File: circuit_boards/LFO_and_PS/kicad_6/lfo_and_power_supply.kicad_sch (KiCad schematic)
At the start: 17 parts, among them J1 AC_power_in, J2 power_out, J3 power_out, J4 power_out, J5 power_out, J6 filter_board_port, U1 TL072

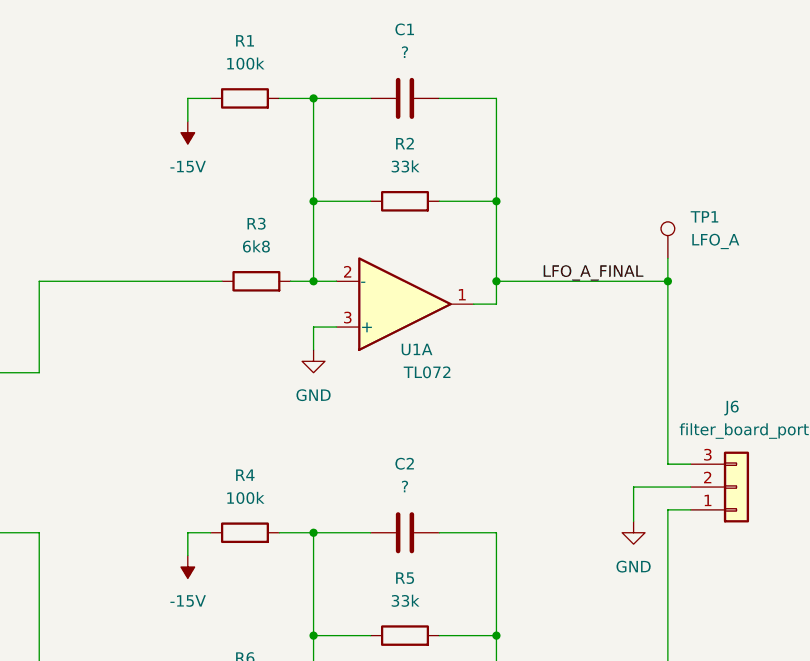
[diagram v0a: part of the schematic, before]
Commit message: Update PCB files, fix VCF mix polarity
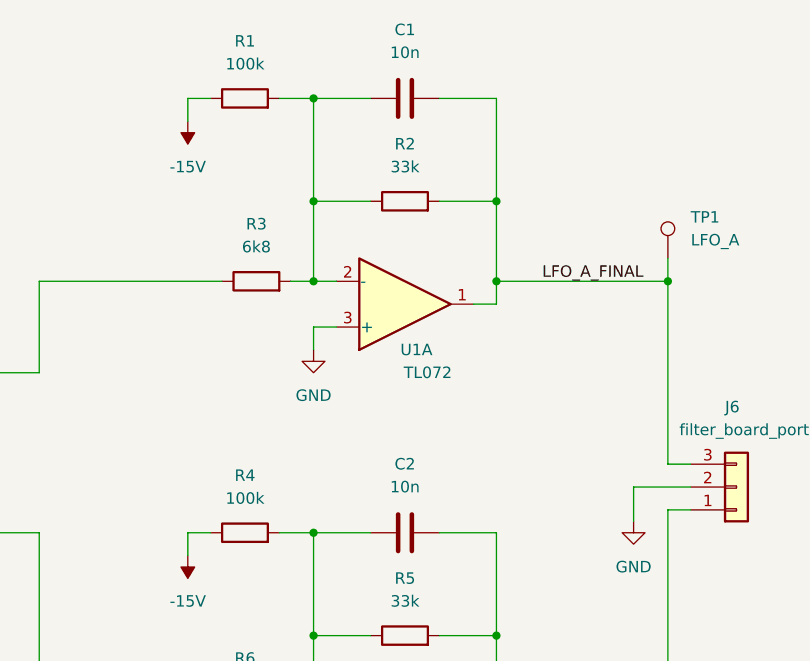
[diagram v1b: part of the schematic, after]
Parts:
- C1, C2: value ? -> 10n
- J1: footprint Connector_Molex:Molex_Mini-Fit_Jr_5566-04A2_2x02_P4.20mm_Vertical -> Connector_Molex:Molex_Mini-Fit_Jr_5566-04A_2x02_P4.20mm_Vertical
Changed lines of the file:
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@@
     (in_bom yes) (on_board yes) (fields_autoplaced)
     (property "Reference" "C2" (id 0) (at 190.5 82.55 90))
-    (property "Value" "?" (id 1) (at 190.5 85.09 90))
+    (property "Value" "10n" (id 1) (at 190.5 85.09 90))
     (property "Footprint" "Capacitor_SMD:C_0805_2012Metric" (id 2) (at 194.31 89.2048 0)
       (effects (font (size 1.27 1.27)) hide)
@@
     (in_bom yes) (on_board yes) (fields_autoplaced)
     (property "Reference" "C1" (id 0) (at 190.5 34.29 90))
-    (property "Value" "?" (id 1) (at 190.5 36.83 90))
+    (property "Value" "10n" (id 1) (at 190.5 36.83 90))
     (property "Footprint" "Capacitor_SMD:C_0805_2012Metric" (id 2) (at 194.31 40.9448 0)
       (effects (font (size 1.27 1.27)) hide)
@@
     (property "Reference" "J1" (id 0) (at 30.48 66.04 0))
     (property "Value" "AC_power_in" (id 1) (at 30.48 68.58 0))
-    (property "Footprint" "Connector_Molex:Molex_Mini-Fit_Jr_5566-04A2_2x02_P4.20mm_Vertical" (id 2) (at 30.48 74.93 0)
+    (property "Footprint" "Connector_Molex:Molex_Mini-Fit_Jr_5566-04A_2x02_P4.20mm_Vertical" (id 2) (at 30.48 74.93 0)
       (effects (font (size 1.27 1.27)) hide)
     )
@@
     )
     (path "/27a532ef-0c09-4c62-bfbb-3624ef1c7dcb"
-      (reference "C1") (unit 1) (value "?") (footprint "Capacitor_SMD:C_0805_2012Metric")
+      (reference "C1") (unit 1) (value "10n") (footprint "Capacitor_SMD:C_0805_2012Metric")
     )
     (path "/05e95b16-6b62-44ea-8a25-dc38df4ba710"
-      (reference "C2") (unit 1) (value "?") (footprint "Capacitor_SMD:C_0805_2012Metric")
+      (reference "C2") (unit 1) (value "10n") (footprint "Capacitor_SMD:C_0805_2012Metric")
     )
     (path "/6cc8d67d-f0af-4522-97bb-c57e963f3f9d/720fda08-e38e-4be5-beaa-b632b67d25fa"
@@
     )
     (path "/4cab5afe-b810-46b3-94ba-f613dce05909/6fab5011-5325-4ae8-afe8-6cd1a3fbb272"
-      (reference "C10") (unit 1) (value "3300u") (footprint "Capacitor_THT:CP_Radial_D17.0mm_P7.50mm")
+      (reference "C10") (unit 1) (value "3300u") (footprint "Capacitor_THT:CP_Radial_D18.0mm_P7.50mm")
     )
     (path "/4cab5afe-b810-46b3-94ba-f613dce05909/ffac9709-5007-4704-8f66-7b36093713ab"
@@
     )
     (path "/4cab5afe-b810-46b3-94ba-f613dce05909/30fa96ad-c9c9-4229-834c-2ec93d10420f"
-      (reference "C14") (unit 1) (value "3300u") (footprint "Capacitor_THT:CP_Radial_D17.0mm_P7.50mm")
+      (reference "C14") (unit 1) (value "3300u") (footprint "Capacitor_THT:CP_Radial_D18.0mm_P7.50mm")
     )
     (path "/4cab5afe-b810-46b3-94ba-f613dce05909/cbd0ff89-c284-432e-8a26-664af57066a8"
@@
     )
     (path "/aa436904-5524-429e-93cc-6d6a65f39f69"
-      (reference "J1") (unit 1) (value "AC_power_in") (footprint "Connector_Molex:Molex_Mini-Fit_Jr_5566-04A2_2x02_P4.20mm_Vertical")
+      (reference "J1") (unit 1) (value "AC_power_in") (footprint "Connector_Molex:Molex_Mini-Fit_Jr_5566-04A_2x02_P4.20mm_Vertical")
     )
     (path "/aeb3b2c9-24f9-4cdf-a26a-8ea198dfa225"
@@
     )
     (path "/6cc8d67d-f0af-4522-97bb-c57e963f3f9d/c1ca5964-b548-4f9e-b8b8-dbc4e7594301"
-      (reference "R7") (unit 1) (value "R") (footprint "Resistor_SMD:R_0805_2012Metric")
+      (reference "R7") (unit 1) (value "10k") (footprint "Resistor_SMD:R_0805_2012Metric")
     )
     (path "/6cc8d67d-f0af-4522-97bb-c57e963f3f9d/db1373b0-0aeb-4604-988a-b51417beff8b"
@@
     )
     (path "/6cc8d67d-f0af-4522-97bb-c57e963f3f9d/e656cab0-5f68-4d01-b288-557c94075e1f"
-      (reference "R9") (unit 1) (value "R") (footprint "Resistor_SMD:R_0805_2012Metric")
+      (reference "R9") (unit 1) (value "15k") (footprint "Resistor_SMD:R_0805_2012Metric")
     )
     (path "/6cc8d67d-f0af-4522-97bb-c57e963f3f9d/6b6485e9-1ce6-438e-ad26-4126954e82f9"
@@
     )
     (path "/6cc8d67d-f0af-4522-97bb-c57e963f3f9d/f61763bd-a46a-4686-a848-6a9239629577"
-      (reference "SW2") (unit 1) (value "SR1712F-0203") (footprint "custom_footprints:SR1712F_rotary_switch")
+      (reference "SW2") (unit 2) (value "SR1712F-0203") (footprint "custom_footprints:SR1712F_rotary_switch")
     )
     (path "/6cc8d67d-f0af-4522-97bb-c57e963f3f9d/06aea827-8cf3-4535-95fc-5955c405c9d7"
